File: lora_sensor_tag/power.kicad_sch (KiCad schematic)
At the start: 57 parts, among them J3 Li-ion_bat_conn, Q1 NPN, U5 TPS63070RNMR, U6 MCP73871-2CAI_ML, U7 AMS1117-3.3, U8 MAX17048G_T10

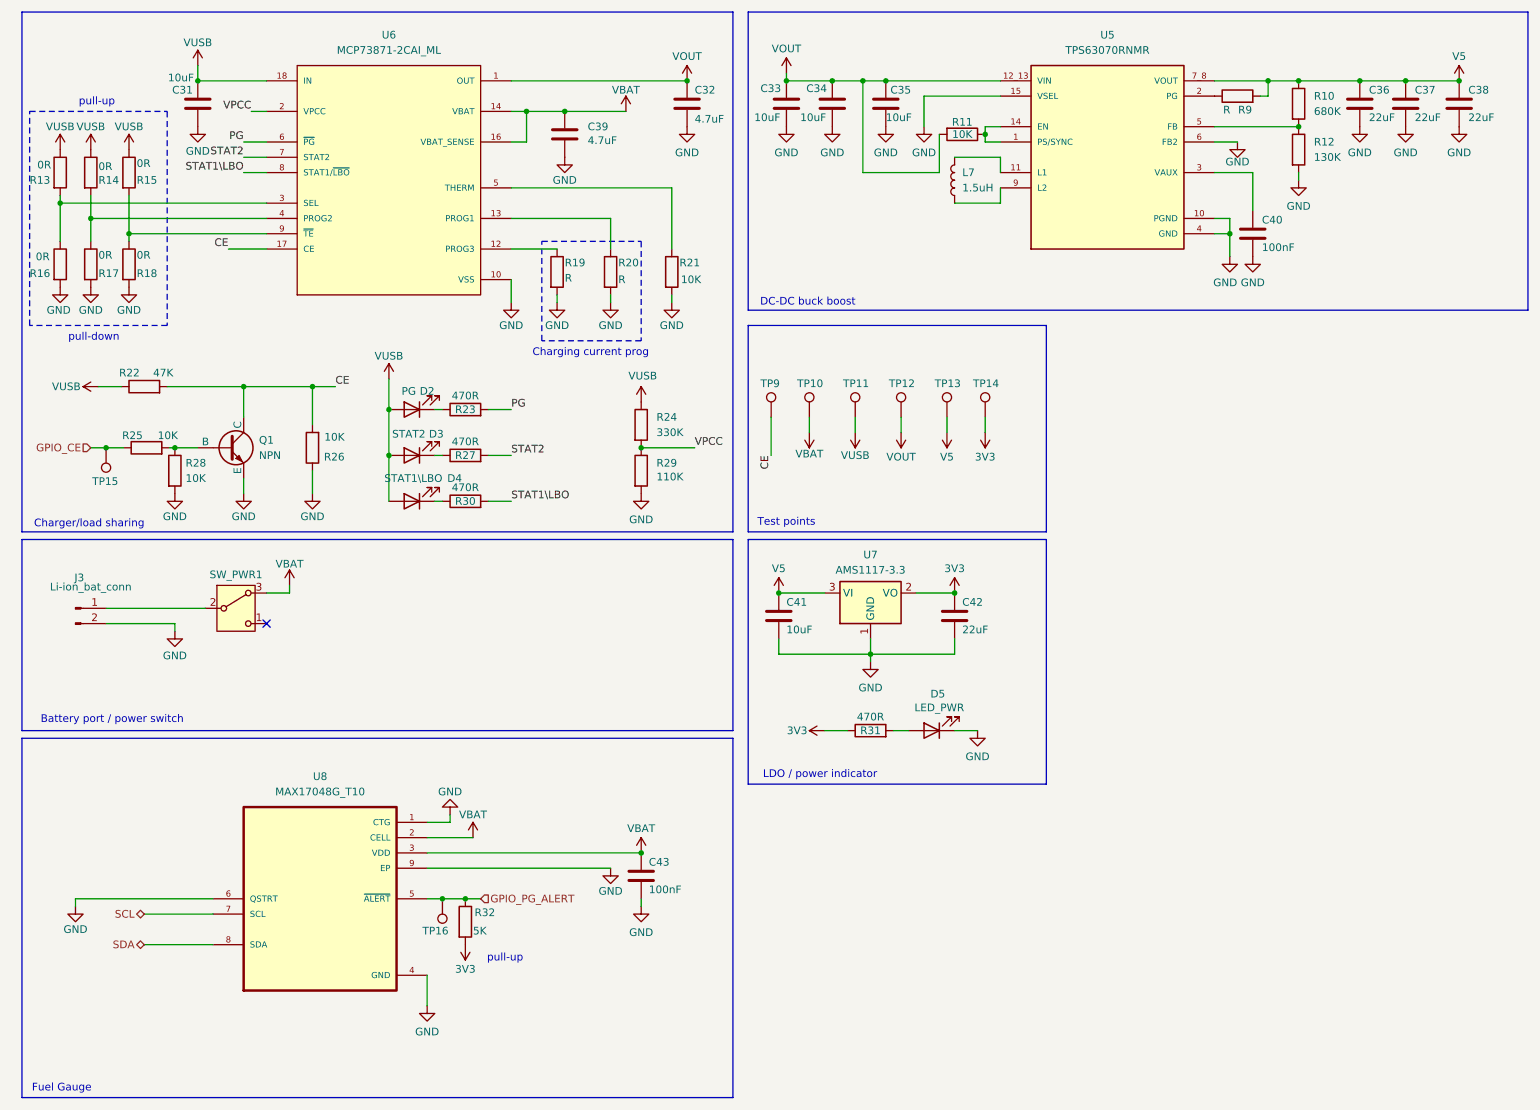
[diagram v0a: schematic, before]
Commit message: DC-DC buckboost to 3V3 using TPS63070. minor fixes to TPS63070 schema.
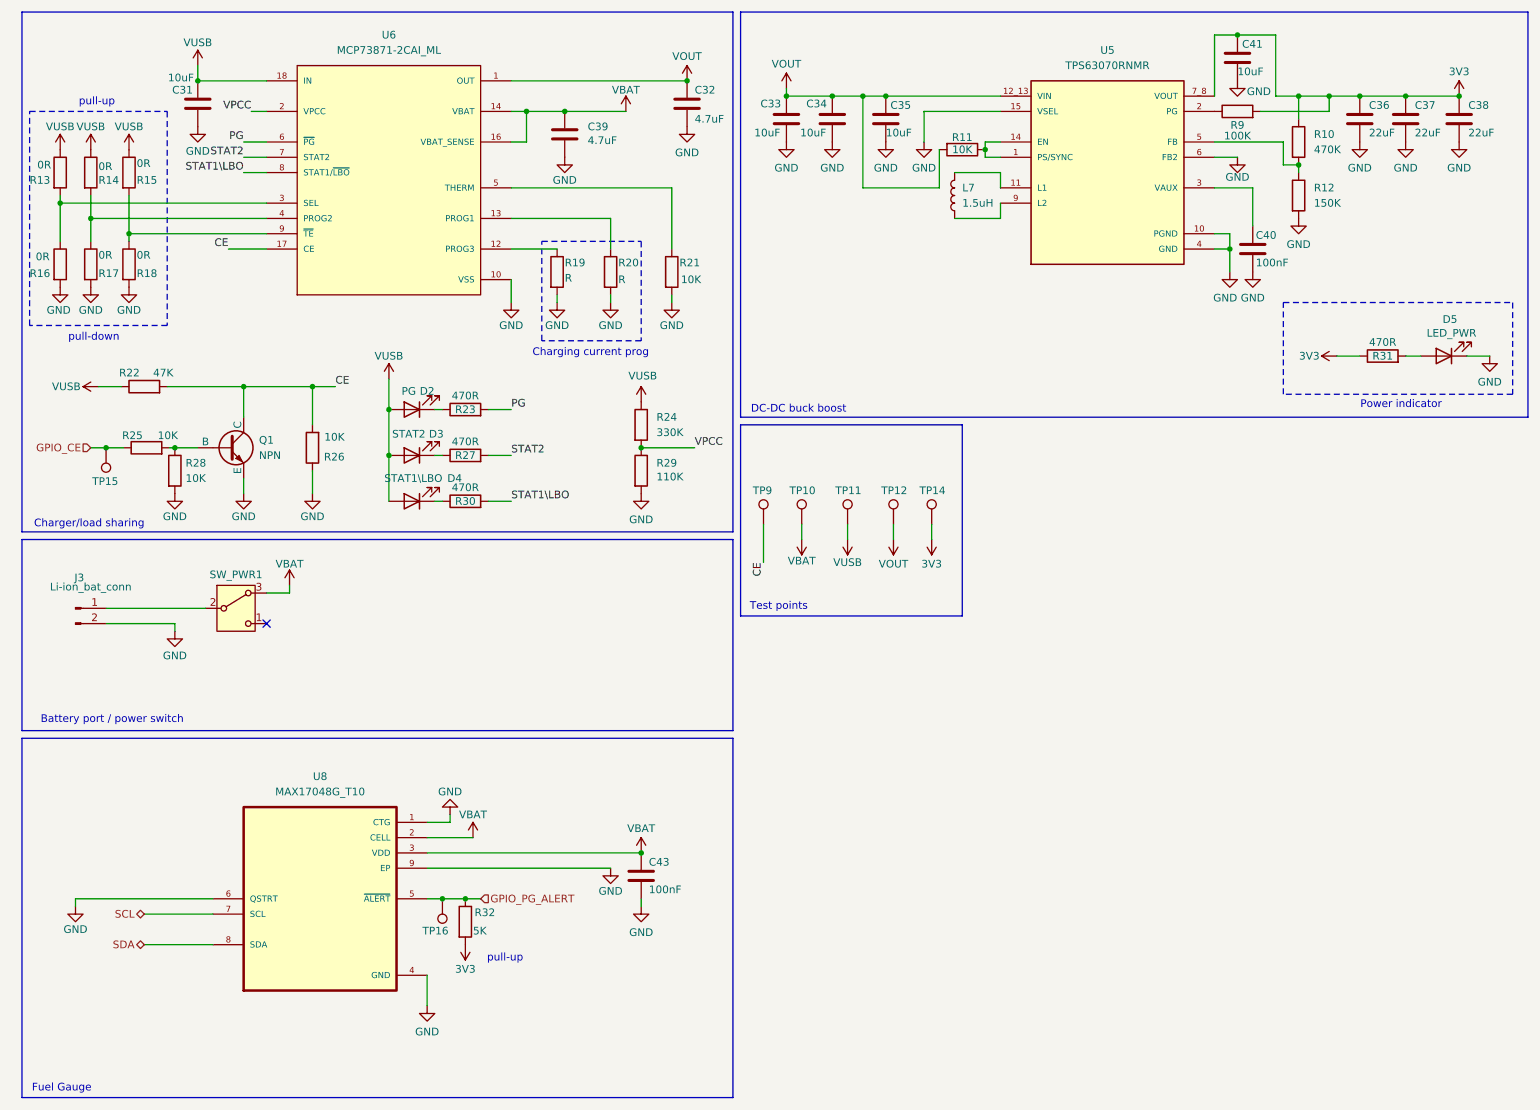
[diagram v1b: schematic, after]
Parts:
- removed C42: 22uF, Capacitor_SMD:C_0603_1608Metric, symbol Device:C
- removed TP13: TestPoint, TestPoint:TestPoint_Pad_D1.0mm, symbol Connector:TestPoint
- removed U7: AMS1117-3.3, Package_TO_SOT_SMD:SOT-223-3_TabPin2, symbol Regulator_Linear:AMS1117-3.3
- R10: value 680K -> 470K
- R12: value 130K -> 150K
- R9: value R -> 100K
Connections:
- net V5 is gone; now on net 3V3: C36.1, C37.1, C38.1, C41.1, R10.1, R9.2, U5.7_8 (VOUT)
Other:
- note added: "Power indicator"
- note removed: "LDO / power indicator"
- moved on the sheet: C33, C34, C35, C36, C37, C38, C40, D5, L7, R10, R11, R12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
